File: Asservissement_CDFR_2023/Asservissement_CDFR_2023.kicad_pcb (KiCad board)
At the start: 2 copper layers, 87 x 115 mm, 165 parts, among them IC1 A3930KJPTR-T, IC2 A3930KJPTR-T, J1 Connecteur batterie, J10 Free Connecteur, J11 Conn_01x02, J12 Conn_01x02, J13 Connecteur Odométrie, J2 Conn_01x03, J3 Conn_01x05, J4 Connecteur Programmation, J5 Conn_01x03, J6 Connecteur Odométrie, J7 Conn_01x03, J8 Conn_01x03, J9 Conn_01x05, Q1 QM6006D, Q10 QM6006D, Q11 QM6006D, Q12 QM6006D, Q13 Q_NMOS_GDS, Q2 QM6006D, Q3 QM6006D, Q4 QM6006D, Q5 QM6006D, Q6 QM6006D, Q7 QM6006D, Q8 QM6006D, Q9 QM6006D, U1 LM317_SOT-223, U3 STM32F401RCTx, U4 LMR16020PDDA, Y1 Crystal_GND24

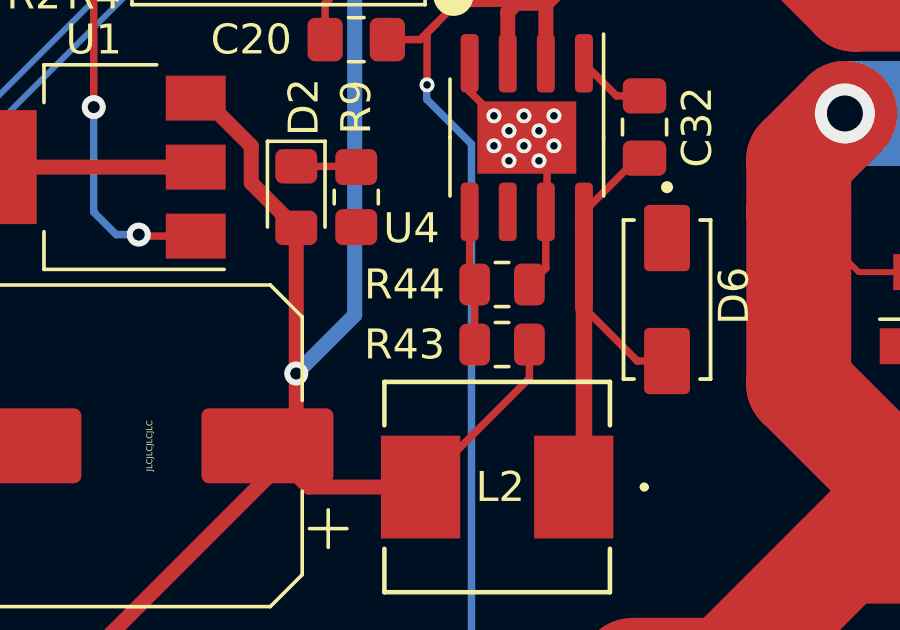
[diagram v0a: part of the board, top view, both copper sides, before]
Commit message: change one resistor
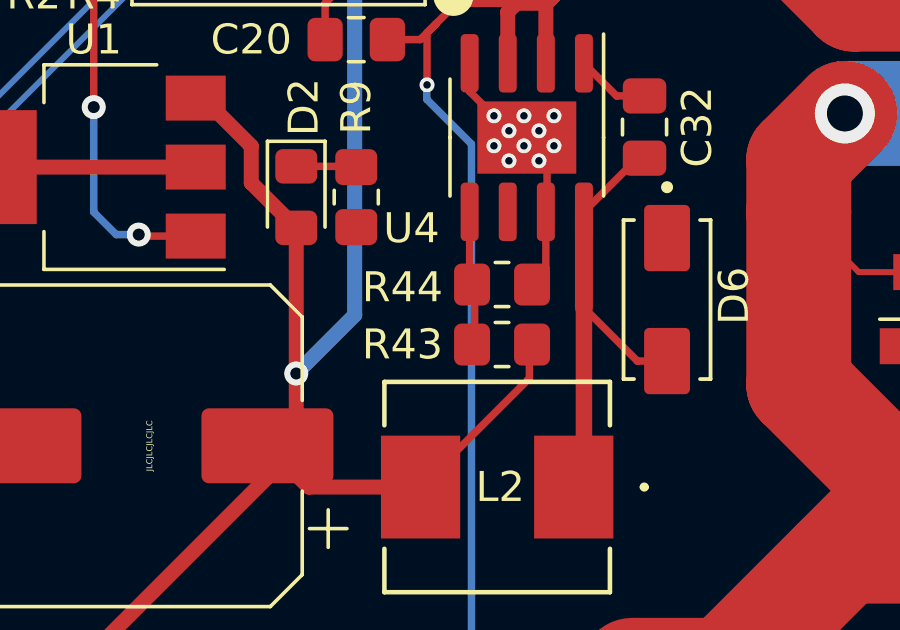
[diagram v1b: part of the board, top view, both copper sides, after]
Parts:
- R18: value 56k -> 390K
- R33: value 56k -> 390k
- R43, R44: footprint Resistor_SMD:R_0805_2012Metric -> Resistor_SMD:R_0805_2012Metric_Pad1.20x1.40mm_HandSolder
